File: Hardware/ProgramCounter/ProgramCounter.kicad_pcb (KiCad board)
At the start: 2 copper layers, 0 parts

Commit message: PC PCB Progress
Mostly done with schematic for the Program Counter. I'll order parts soon and start on the PCB design next. It'll be my first four layer board!

Based on what I've seen so far, CMOS seems to be more prevalent than TTL, so I'll make this computer out of CMOS.
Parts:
- added C1: .1uF, Capacitor_SMD:C_1206_3216Metric_Pad1.42x1.75mm_HandSolder, F.Cu at (152.4, 100.7)
- added C10: .1uF, Capacitor_SMD:C_1206_3216Metric_Pad1.42x1.75mm_HandSolder, F.Cu at (186.5, 85.8)
- added C11: .1uF, Capacitor_SMD:C_1206_3216Metric_Pad1.42x1.75mm_HandSolder, F.Cu at (186.5, 75.9)
- added C12: .1uF, Capacitor_SMD:C_1206_3216Metric_Pad1.42x1.75mm_HandSolder, F.Cu at (186.5, 103.6)
- added C13: .1uF, Capacitor_SMD:C_1206_3216Metric_Pad1.42x1.75mm_HandSolder, F.Cu at (186.5, 100.3)
- added C14: .1uF, Capacitor_SMD:C_1206_3216Metric_Pad1.42x1.75mm_HandSolder, F.Cu at (186.5, 97.0)
- added C15: .1uF, Capacitor_SMD:C_1206_3216Metric_Pad1.42x1.75mm_HandSolder, F.Cu at (186.5, 93.7)
- added C2: .1uF, Capacitor_SMD:C_1206_3216Metric_Pad1.42x1.75mm_HandSolder, F.Cu at (171.0, 110.2)
- added C3: .1uF, Capacitor_SMD:C_1206_3216Metric_Pad1.42x1.75mm_HandSolder, F.Cu at (119.6, 96.5)
- added C4: .1uF, Capacitor_SMD:C_1206_3216Metric_Pad1.42x1.75mm_HandSolder, F.Cu at (162.3, 76.1)
- added C5: .1uF, Capacitor_SMD:C_1206_3216Metric_Pad1.42x1.75mm_HandSolder, F.Cu at (119.6, 99.8)
- added C6: .1uF, Capacitor_SMD:C_1206_3216Metric_Pad1.42x1.75mm_HandSolder, F.Cu at (162.8, 103.2)
- added C7: .1uF, Capacitor_SMD:C_1206_3216Metric_Pad1.42x1.75mm_HandSolder, F.Cu at (125.6, 100.2)
- added C8: .1uF, Capacitor_SMD:C_1206_3216Metric_Pad1.42x1.75mm_HandSolder, F.Cu at (186.5, 79.2)
- added C9: .1uF, Capacitor_SMD:C_1206_3216Metric_Pad1.42x1.75mm_HandSolder, F.Cu at (186.5, 82.5)
- added J1: Conn_02x16_Counter_Clockwise, Connector_PinHeader_2.54mm:PinHeader_2x16_P2.54mm_Horizontal, F.Cu at (197.6, 119.9)
- added J2: Conn_02x16_Counter_Clockwise, Connector_PinHeader_2.54mm:PinHeader_2x16_P2.54mm_Horizontal, F.Cu at (155.0, 120.0)
- added UADD1: 74LS283, Package_SO:TSSOP-16_4.4x5mm_P0.65mm, F.Cu at (179.0, 84.5)
- added UADD2: 74LS283, Package_SO:TSSOP-16_4.4x5mm_P0.65mm, F.Cu at (179.0, 77.7)
- added UADD3: 74LS283, Package_SO:TSSOP-16_4.4x5mm_P0.65mm, F.Cu at (170.1, 77.7)
- added UADD4: 74LS283, Package_SO:TSSOP-16_4.4x5mm_P0.65mm, F.Cu at (170.1, 84.5)
- added UCMP1: 74LS684, Package_SO:SSOP-20_3.9x8.7mm_P0.635mm, F.Cu at (157.2, 114.3)
- added UCONDMUX1: 74151, Package_SO:SOP-16_4.55x10.3mm_P1.27mm, F.Cu at (154.3, 80.4)
- added UMUX0: 74LS257, Package_SO:TSSOP-16_4.4x5mm_P0.65mm, F.Cu at (170.1, 95.5)
- added UMUX1: 74LS257, Package_SO:TSSOP-16_4.4x5mm_P0.65mm, F.Cu at (170.1, 102.2)
- added UMUX2: 74LS257, Package_SO:TSSOP-16_4.4x5mm_P0.65mm, F.Cu at (179.0, 95.5)
- added UMUX3: 74LS257, Package_SO:TSSOP-16_4.4x5mm_P0.65mm, F.Cu at (179.0, 102.2)
- added UNAND1: 74LS00, Package_SO:TSSOP-14_4.4x5mm_P0.65mm, F.Cu at (134.2, 99.5)
- added UPR0: 74HCT273, Package_SO:SOIC-20W_7.5x12.8mm_P1.27mm, F.Cu at (138.1, 110.7)
- added UPR1: 74HCT273, Package_SO:SOIC-20W_7.5x12.8mm_P1.27mm, F.Cu at (122.2, 110.9)
- added UQAND1: 74LS21, Package_SO:MSOP-12_3x4mm_P0.65mm, F.Cu at (144.9, 82.9)
- added UXOR1: 74HC86, Package_SO:SOIC-14_3.9x8.7mm_P1.27mm, F.Cu at (145.7, 100.5)
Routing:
- net /IMM3: track 0.00 -> 116.2 mm, vias 0 -> 18
- net GND: track 0.00 -> 30.2 mm, vias 0 -> 5
- net (no net): track 0.00 -> 24.5 mm, vias 0 -> 1
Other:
- copper layers 2 -> 4

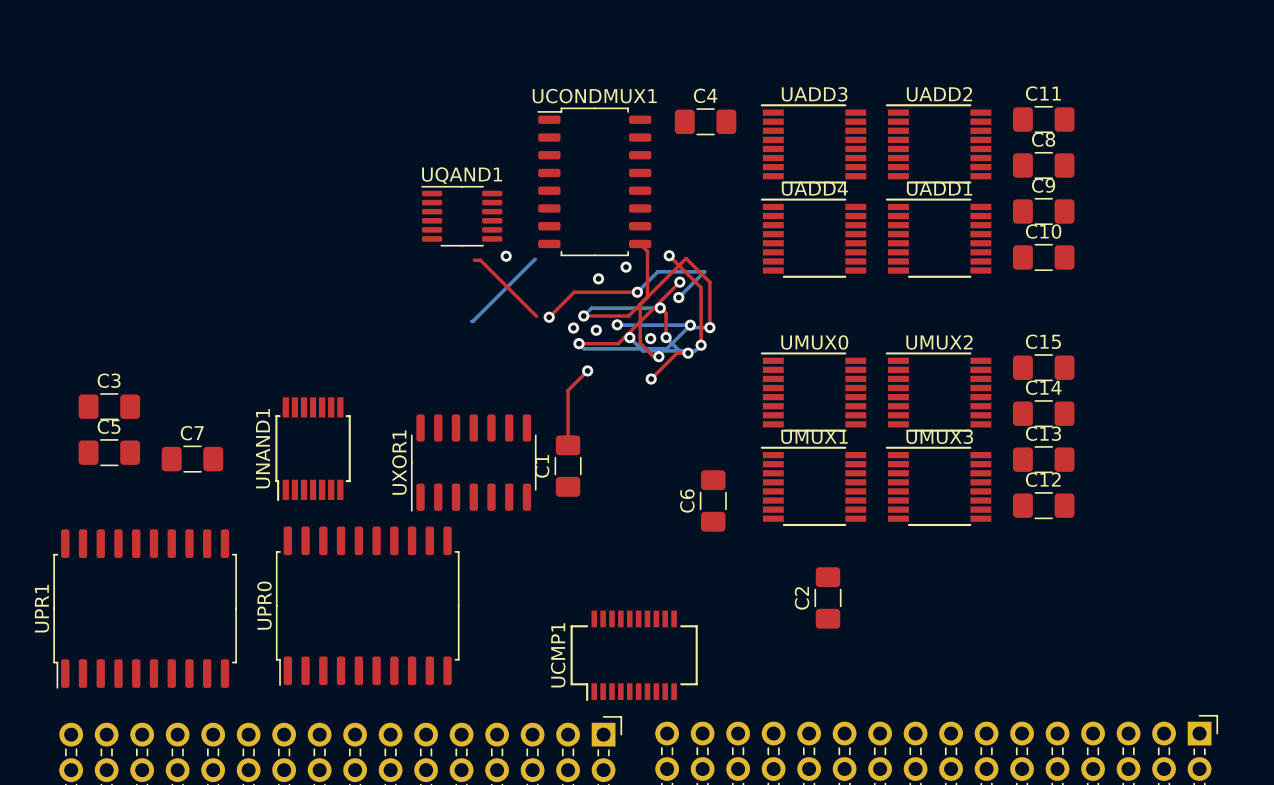
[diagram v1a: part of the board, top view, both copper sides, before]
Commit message: PC Schematic
Mostly finished Program Counter schematic. I'm basing the hardware largely off of TI's new HCS family of SN74HCS chips.
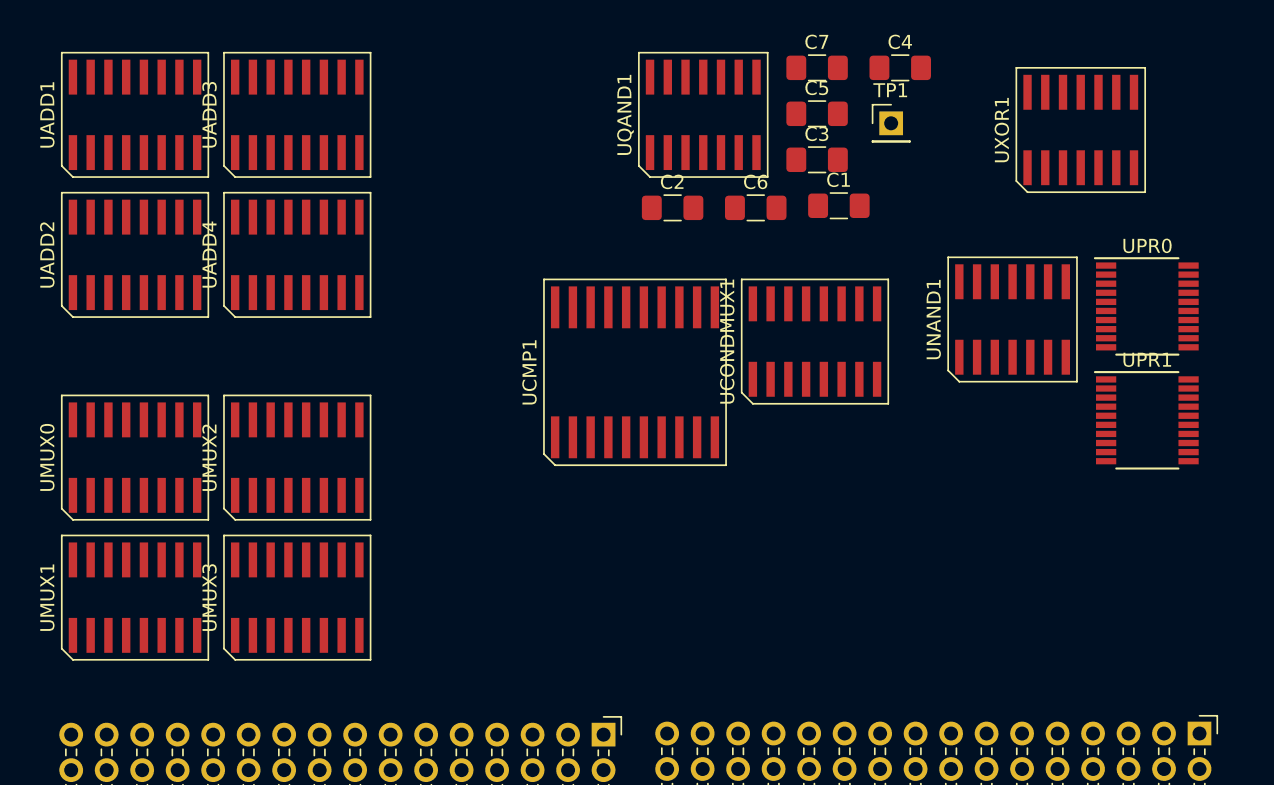
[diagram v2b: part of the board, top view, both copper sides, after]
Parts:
- removed C10, C11, C12, C13, C14, C15, C8, C9: .1uF, Capacitor_SMD:C_1206_3216Metric_Pad1.42x1.75mm_HandSolder
- added TP1: TP_PCEVENT, Connector_PinHeader_2.54mm:PinHeader_1x01_P2.54mm_Vertical, F.Cu at (175.6, 76.2)
- UADD1, UADD2, UADD3, UADD4: footprint Package_SO:TSSOP-16_4.4x5mm_P0.65mm -> aFootprint:R-PDSO-G16
- UCMP1: footprint Package_SO:SSOP-20_3.9x8.7mm_P0.635mm -> aFootprint:DW0020A
- UCONDMUX1: footprint Package_SO:SOP-16_4.55x10.3mm_P1.27mm -> aFootprint:R-PDSO-G16
- UMUX0, UMUX1, UMUX2, UMUX3: value 74LS257 -> 74LS157; footprint Package_SO:TSSOP-16_4.4x5mm_P0.65mm -> aFootprint:R-PDSO-G16
- UNAND1: footprint Package_SO:TSSOP-14_4.4x5mm_P0.65mm -> aFootprint:R-PDSO-G14
- UPR0, UPR1: footprint Package_SO:SOIC-20W_7.5x12.8mm_P1.27mm -> Package_SO:TSSOP-20_4.4x6.5mm_P0.65mm
- UQAND1: footprint Package_SO:MSOP-12_3x4mm_P0.65mm -> aFootprint:R-PDSO-G14
- UXOR1: footprint Package_SO:SOIC-14_3.9x8.7mm_P1.27mm -> aFootprint:R-PDSO-G14
- moved UPR1 73.0 mm to (193.9, 97.5), turned to 0 degrees
- moved UPR0 59.8 mm to (193.9, 89.3), turned to 0 degrees
- moved UADD1 58.3 mm to (121.5, 75.6)
- moved UADD2 58.1 mm to (121.5, 85.6)
- moved C5 56.2 mm to (170.3, 75.5)
- moved C3 53.6 mm to (170.3, 78.8)
- moved C7 52.7 mm to (170.3, 72.2)
- moved UNAND1 50.9 mm to (184.2, 90.2), turned to 0 degrees
- moved UXOR1 49.5 mm to (189.1, 76.7), turned to 0 degrees
- moved UMUX1 49.3 mm to (121.5, 110.2)
- moved UMUX0 48.9 mm to (121.5, 100.1)
- moved UMUX3 46.6 mm to (133.1, 110.2)
- moved UMUX2 46.2 mm to (133.1, 100.1)
- moved UADD3 37.1 mm to (133.1, 75.6)
- moved UADD4 37.0 mm to (133.1, 85.6)
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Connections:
- net /IS_JMP renamed /~IS_JMP
- UADD1 pad 3: /16 Bit Adder/COUNT+2 -> /IS_SKIP
- UADD1 pad 5: /IS_SKIP -> /~IS_SKIP
- UMUX0 pad 10: /REGMEM3 -> /16 Bit Adder/COUT2
- UMUX0 pad 11: /16 Bit Adder/COUT3 -> /REGMEM2
- UMUX0 pad 12: /16x 2to1 Mux/OUT2 -> /NEXTPC3
- UMUX0 pad 13: /REGMEM2 -> /16 Bit Adder/COUT3
- UMUX0 pad 14: /16 Bit Adder/COUT2 -> /REGMEM3
- UMUX0 pad 15: /16x 2to1 Mux/~OE -> GND
- UMUX0 pad 2: /16 Bit Adder/COUT0 -> /REGMEM0
- UMUX0 pad 3: /REGMEM0 -> /16 Bit Adder/COUT0
- UMUX0 pad 4: /16x 2to1 Mux/OUT0 -> /NEXTPC0
- UMUX0 pad 5: /16 Bit Adder/COUT1 -> /REGMEM1
- UMUX0 pad 6: /REGMEM1 -> /16 Bit Adder/COUT1
- UMUX0 pad 7: /16x 2to1 Mux/OUT1 -> /NEXTPC1
- UMUX0 pad 9: /16x 2to1 Mux/OUT3 -> /NEXTPC2
- UMUX1 pad 10: /REGMEM7 -> /16 Bit Adder/COUT6
- UMUX1 pad 11: /16 Bit Adder/COUT7 -> /REGMEM6
- UMUX1 pad 12: /16x 2to1 Mux/OUT6 -> /NEXTPC7
- UMUX1 pad 13: /REGMEM6 -> /16 Bit Adder/COUT7
- UMUX1 pad 14: /16 Bit Adder/COUT6 -> /REGMEM7
- UMUX1 pad 15: /16x 2to1 Mux/~OE -> GND
- UMUX1 pad 2: /16 Bit Adder/COUT4 -> /REGMEM4
- UMUX1 pad 3: /REGMEM4 -> /16 Bit Adder/COUT4
- UMUX1 pad 4: /16x 2to1 Mux/OUT4 -> /NEXTPC4
- UMUX1 pad 5: /16 Bit Adder/COUT5 -> /REGMEM5
- UMUX1 pad 6: /REGMEM5 -> /16 Bit Adder/COUT5
- UMUX1 pad 7: /16x 2to1 Mux/OUT5 -> /NEXTPC5
- UMUX1 pad 9: /16x 2to1 Mux/OUT7 -> /NEXTPC6
- UMUX2 pad 10: /REGMEM11 -> /16 Bit Adder/COUT10
- UMUX2 pad 11: /16 Bit Adder/COUT11 -> /REGMEM10
- UMUX2 pad 12: /16x 2to1 Mux/OUT6 -> /NEXTPC11
- UMUX2 pad 13: /REGMEM10 -> /16 Bit Adder/COUT11
- UMUX2 pad 14: /16 Bit Adder/COUT10 -> /REGMEM11
- UMUX2 pad 15: /16x 2to1 Mux/~OE -> GND
- UMUX2 pad 2: /16 Bit Adder/COUT8 -> /REGMEM8
- UMUX2 pad 3: /REGMEM8 -> /16 Bit Adder/COUT8
- UMUX2 pad 4: /16x 2to1 Mux/OUT4 -> /NEXTPC8
- UMUX2 pad 5: /16 Bit Adder/COUT9 -> /REGMEM9
- UMUX2 pad 6: /REGMEM9 -> /16 Bit Adder/COUT9
- UMUX2 pad 7: /16x 2to1 Mux/OUT5 -> /NEXTPC9
- UMUX2 pad 9: /16x 2to1 Mux/OUT7 -> /NEXTPC10
- UMUX3 pad 10: /REGMEM15 -> /16 Bit Adder/COUT14
- UMUX3 pad 11: /16 Bit Adder/COUT15 -> /REGMEM14
- UMUX3 pad 12: /16x 2to1 Mux/OUT6 -> /NEXTPC15
- UMUX3 pad 13: /REGMEM14 -> /16 Bit Adder/COUT15
- UMUX3 pad 14: /16 Bit Adder/COUT14 -> /REGMEM15
- UMUX3 pad 15: /16x 2to1 Mux/~OE -> GND
- UMUX3 pad 2: /16 Bit Adder/COUT12 -> /REGMEM12
- UMUX3 pad 3: /REGMEM12 -> /16 Bit Adder/COUT12
- UMUX3 pad 4: /16x 2to1 Mux/OUT4 -> /NEXTPC12
- UMUX3 pad 5: /16 Bit Adder/COUT13 -> /REGMEM13
- UMUX3 pad 6: /REGMEM13 -> /16 Bit Adder/COUT13
- UMUX3 pad 7: /16x 2to1 Mux/OUT5 -> /NEXTPC13
- UMUX3 pad 9: /16x 2to1 Mux/OUT7 -> /NEXTPC14
- UNAND1 pad 10: /OPCODE1 -> VCC
- UNAND1 pad 12: Net-(UNAND1-Pad12) -> /PCEVENT
- UNAND1 pad 13: Net-(UNAND1-Pad13) -> /JINST
- UNAND1 pad 4: /OPCODE0 -> /PCEVENT
- UNAND1 pad 5: Net-(UNAND1-Pad12) -> /SINST
- UNAND1 pad 6: /IS_SKIP -> /~IS_SKIP
- UNAND1 pad 8: Net-(UNAND1-Pad8) -> /IS_SKIP
- UNAND1 pad 9: VCC -> /~IS_SKIP
- UQAND1 pad 1: Net-(UNAND1-Pad8) -> /OPCODE0
- UQAND1 pad 10: VCC -> /~OPCODE1
- UQAND1 pad 12: VCC -> /OPCODE2
- UQAND1 pad 2: /OPCODE2 -> /~OPCODE1
- UQAND1 pad 4: /OPCODE3 -> /OPCODE2
- UQAND1 pad 5: Net-(UQAND1-Pad5) -> /OPCODE3
- UQAND1 pad 6: Net-(UNAND1-Pad12) -> /JINST
- UQAND1 pad 8: Net-(UQAND1-Pad8) -> /SINST
- UQAND1 pad 9: VCC -> /~OPCODE0
- UXOR1 pad 3: Net-(UQAND1-Pad5) -> /PCEVENT
- UXOR1 pad 6: Net-(UNAND1-Pad13) -> /~OPCODE0
- UXOR1 pad 8: /16 Bit Adder/COUNT+2 -> /~OPCODE1
- UXOR1 pad 9: /IS_SKIP -> /OPCODE1
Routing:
- net /IMM3: track 116.2 -> 0.00 mm, vias 18 -> 0
- net GND: track 30.2 -> 0.00 mm, vias 5 -> 0
- net (no net): track 24.5 -> 0.00 mm, vias 1 -> 0
